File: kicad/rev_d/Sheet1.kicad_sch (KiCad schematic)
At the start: 159 parts, among them J1 JUMPER, J2 JUMPER, J3 JUMPER, J4 JUMPER, J7 JUMPER, Q1 QUARTZ, X1 FDD34M, X2 IDE40M, X3 IDC26LPT, X7 DB15VGA, X8 PLB1-4I, X9 PLB1-2

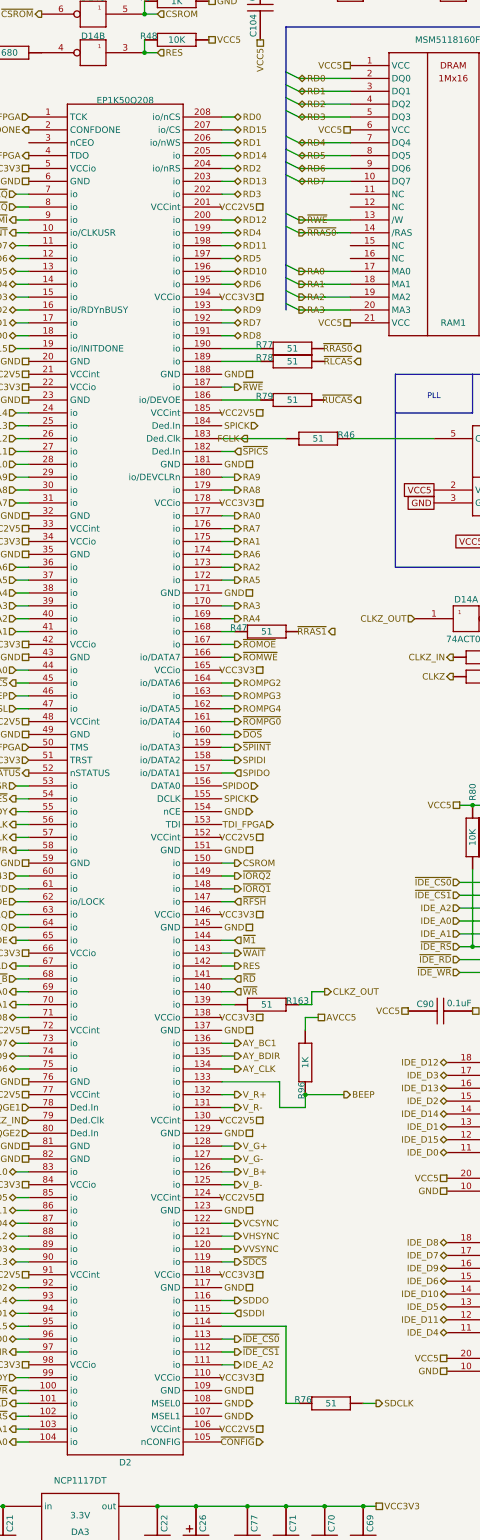
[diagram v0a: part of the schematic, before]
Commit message: pentevo: small update to converted kicad sch (FPGA)
git-svn-id: svn://localhost/local-pentevo@1173 c6c76956-fad2-4150-a3a9-ea0a427205ba
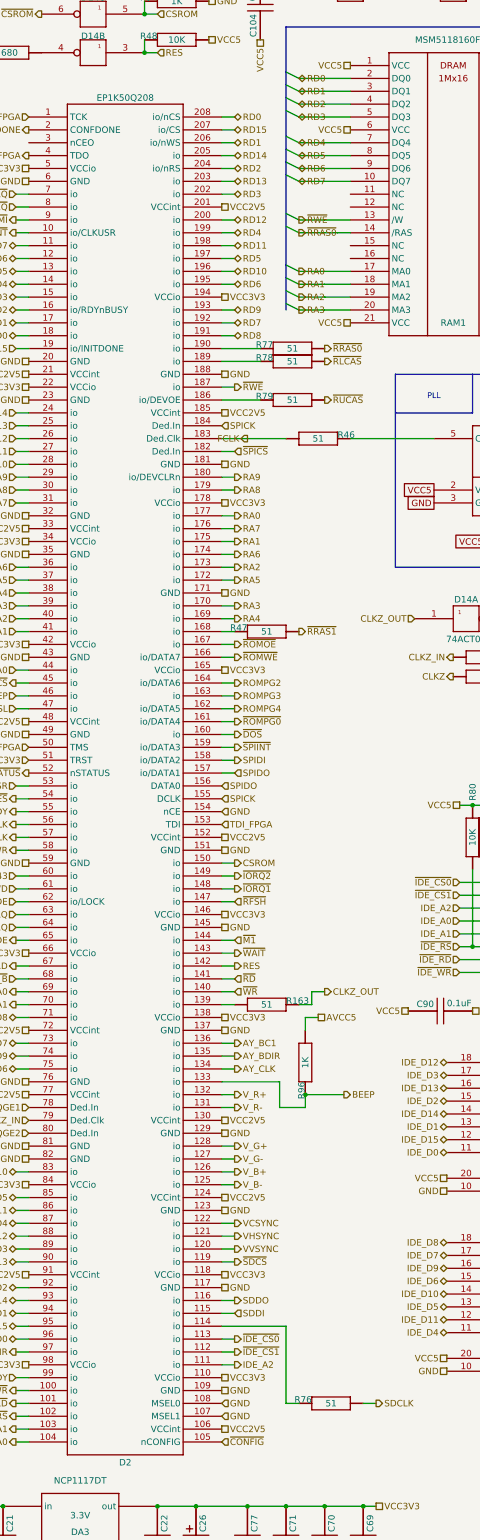
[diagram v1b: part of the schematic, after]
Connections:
- net GND: now also D2.107 (MSEL1), D2.108 (MSEL0), D2.109 (GND), D2.117 (GND), D2.123 (GND), D2.129 (GND), D2.137 (GND), D2.145 (GND), D2.151 (GND), D2.154 (nCE), D2.171 (GND), D2.181 (GND), D2.188 (GND)
- net SPICK: now also D2.155 (DCLK), D2.184 (Ded.In)
- net SPIDO: now also D2.156 (DATA0)
- net TDI_FPGA: now also D2.153 (TDI)
- net VCC2V5: now also D2.106 (VCCint), D2.124 (VCCint), D2.130 (VCCint), D2.152 (VCCint), D2.185 (VCCint), D2.201 (VCCint)
- net VCC3V3: now also D2.110 (VCCio), D2.118 (VCCio), D2.138 (VCCio), D2.146 (VCCio), D2.165 (VCCio), D2.178 (VCCio), D2.194 (VCCio)
- net ~{CONFIG}: now also D2.105 (nCONFIG)
- net ~{RLCAS}: now also R78.1 (i/o)
- net ~{RRAS0}: now also R77.1 (i/o)
- net ~{RRAS1}: now also R47.1 (i/o)
- net ~{RUCAS}: now also R79.1 (i/o)

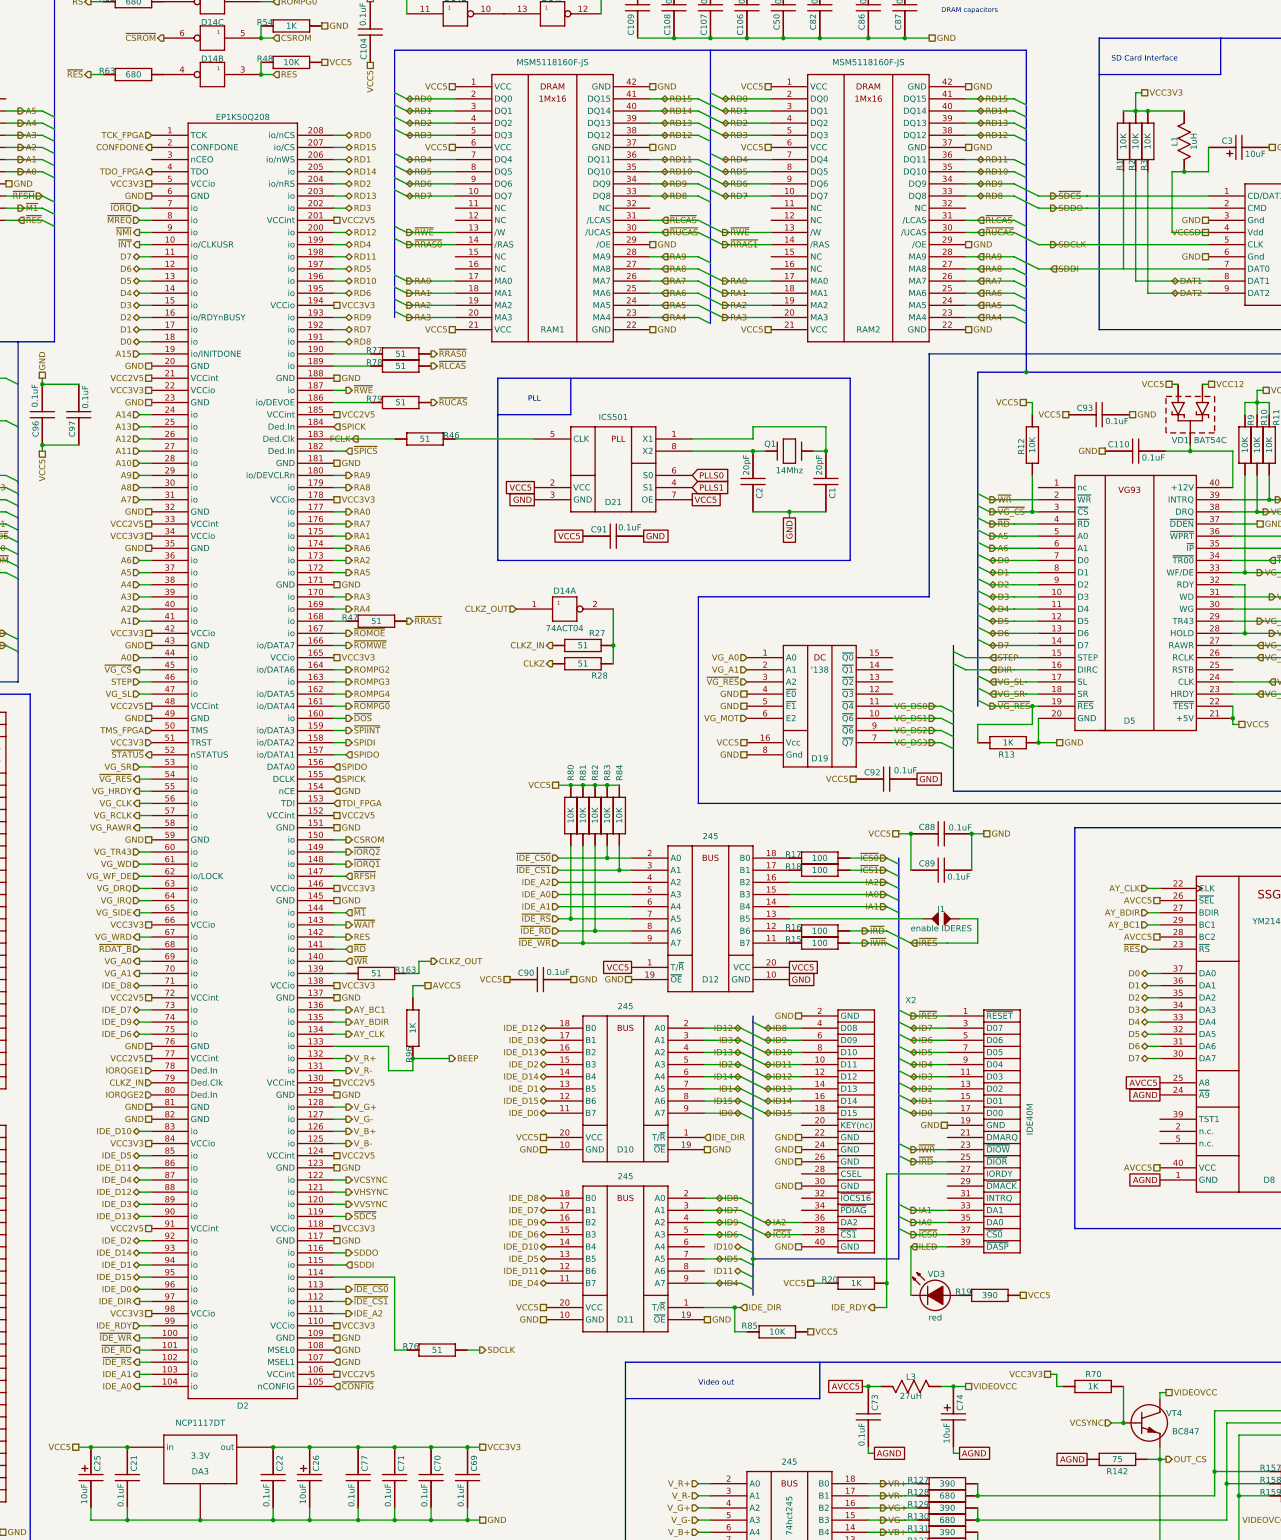
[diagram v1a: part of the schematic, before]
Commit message: pentevo: small update to converted kicad sch (RTC, pgm conns)
git-svn-id: svn://localhost/local-pentevo@1175 c6c76956-fad2-4150-a3a9-ea0a427205ba
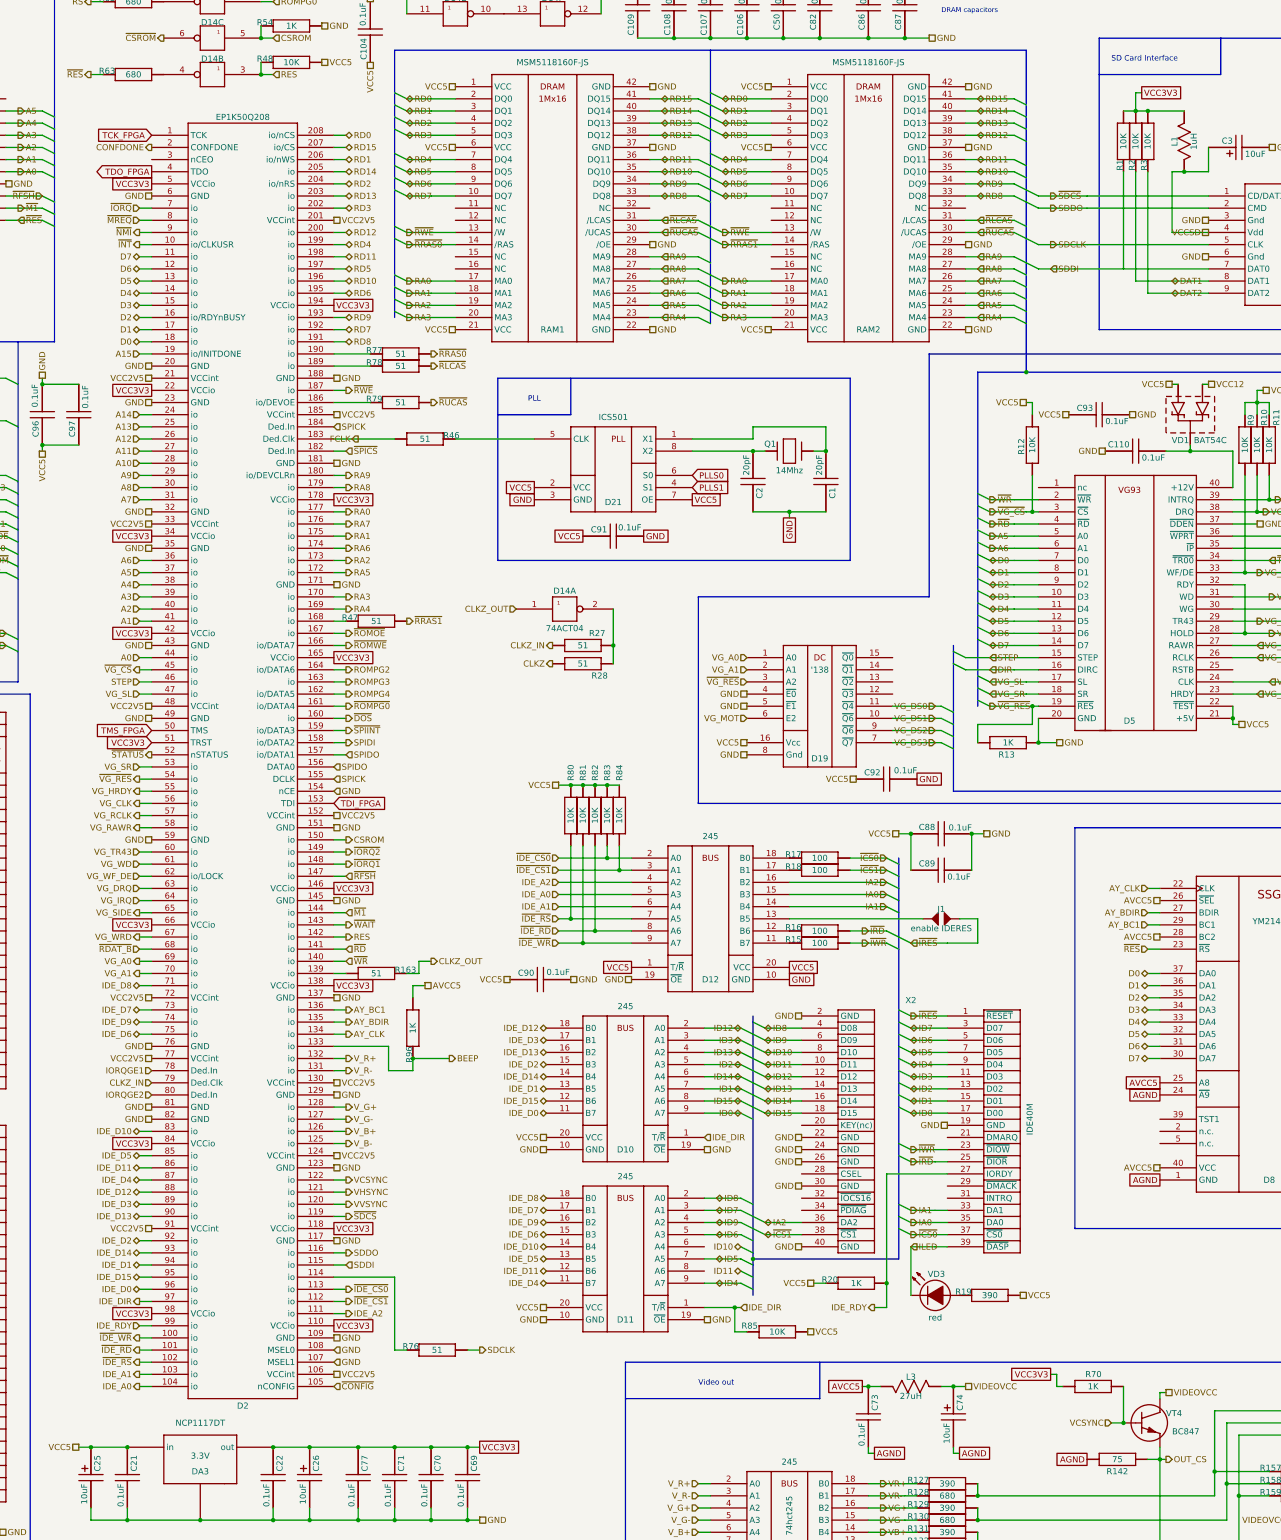
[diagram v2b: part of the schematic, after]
